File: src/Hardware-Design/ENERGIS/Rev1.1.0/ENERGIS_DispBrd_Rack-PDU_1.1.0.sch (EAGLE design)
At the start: 78 parts, among them CON1 DNI, CON2 AFC11-S20ICC-00, IC1 MCP23017T-E/ML, IC2 MCP23017T-E/ML, T1 DNI

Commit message: general update for the repo
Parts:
- R4: value DNI -> 10K 1%
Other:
- moved on the sheet: DSP
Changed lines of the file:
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@@
 <part name="P+3" library="ds_passive" deviceset="+5V" device=""/>
 <part name="R5" library="ds_resistor" deviceset="33K-1%" device="0402" package3d_urn="urn:adsk.eagle:package:46683744/3" value="33K 1%"/>
-<part name="C7" library="ds_capacitors" deviceset="100NF-25V" device="-0402" package3d_urn="urn:adsk.eagle:package:46766485/3" value="100nF 25V"/>
+<part name="C7" library="ds_capacitors" deviceset="100NF-25V" device="-0402" package3d_urn="urn:adsk.eagle:package:46766485/4" value="100nF 25V"/>
 <part name="GND13" library="ds_passive" deviceset="GND" device=""/>
 <part name="GND17" library="ds_passive" deviceset="GND" device=""/>
 <part name="+3V310" library="ds_passive" deviceset="+3V3" device=""/>
 <part name="R6" library="ds_resistor" deviceset="33K-1%" device="0402" package3d_urn="urn:adsk.eagle:package:46683744/3" value="33K 1%"/>
-<part name="C8" library="ds_capacitors" deviceset="100NF-25V" device="-0402" package3d_urn="urn:adsk.eagle:package:46766485/3" value="100nF 25V"/>
+<part name="C8" library="ds_capacitors" deviceset="100NF-25V" device="-0402" package3d_urn="urn:adsk.eagle:package:46766485/4" value="100nF 25V"/>
 <part name="GND14" library="ds_passive" deviceset="GND" device=""/>
 <part name="GND18" library="ds_passive" deviceset="GND" device=""/>
 <part name="+3V311" library="ds_passive" deviceset="+3V3" device=""/>
 <part name="R12" library="ds_resistor" deviceset="33K-1%" device="0402" package3d_urn="urn:adsk.eagle:package:46683744/3" value="33K 1%"/>
-<part name="C9" library="ds_capacitors" deviceset="100NF-25V" device="-0402" package3d_urn="urn:adsk.eagle:package:46766485/3" value="100nF 25V"/>
+<part name="C9" library="ds_capacitors" deviceset="100NF-25V" device="-0402" package3d_urn="urn:adsk.eagle:package:46766485/4" value="100nF 25V"/>
 <part name="GND19" library="ds_passive" deviceset="GND" device=""/>
 <part name="GND22" library="ds_passive" deviceset="GND" device=""/>
@@
 <part name="+3V38" library="ds_passive" deviceset="+3V3" device=""/>
 <part name="+3V39" library="ds_passive" deviceset="+3V3" device=""/>
-<part name="C5" library="ds_capacitors" deviceset="100NF-25V" device="-0402" package3d_urn="urn:adsk.eagle:package:46766485/3" value="100nF 25V"/>
-<part name="C6" library="ds_capacitors" deviceset="100NF-25V" device="-0402" package3d_urn="urn:adsk.eagle:package:46766485/3" value="100nF 25V"/>
+<part name="C5" library="ds_capacitors" deviceset="100NF-25V" device="-0402" package3d_urn="urn:adsk.eagle:package:46766485/4" value="100nF 25V"/>
+<part name="C6" library="ds_capacitors" deviceset="100NF-25V" device="-0402" package3d_urn="urn:adsk.eagle:package:46766485/4" value="100nF 25V"/>
 <part name="GND12" library="ds_passive" deviceset="GND" device=""/>
 <part name="GND11" library="ds_passive" deviceset="GND" device=""/>
@@
 <part name="NC7" library="ds_passive" library_urn="urn:adsk.eagle:library:46685041" deviceset="NC" device=""/>
 <part name="NC5" library="ds_passive" deviceset="NC" device=""/>
-<part name="R4" library="ds_resistor" deviceset="10K-1%" device="0402" package3d_urn="urn:adsk.eagle:package:46683744/3" value="DNI"/>
+<part name="R4" library="ds_resistor" deviceset="10K-1%" device="0402" package3d_urn="urn:adsk.eagle:package:46683744/3" value="10K 1%"/>
 <part name="GND7" library="ds_passive" deviceset="GND" device=""/>
 <part name="NC8" library="ds_passive" deviceset="NC" device=""/>
-<part name="3V3" library="ds_passive" deviceset="TP" device="-ROUND" value="DNI"/>
-<part name="5V" library="ds_passive" deviceset="TP" device="-ROUND" value="DNI"/>
-<part name="BL" library="ds_passive" deviceset="TP" device="-ROUND" value="DNI"/>
-<part name="GND" library="ds_passive" deviceset="TP" device="-ROUND" value="DNI"/>
+<part name="3V3" library="ds_passive" deviceset="TP" device="-ROUND" package3d_urn="urn:adsk.eagle:package:50081795/1" value="DNI"/>
+<part name="5V" library="ds_passive" deviceset="TP" device="-ROUND" package3d_urn="urn:adsk.eagle:package:50081795/1" value="DNI"/>
+<part name="BL" library="ds_passive" deviceset="TP" device="-ROUND" package3d_urn="urn:adsk.eagle:package:50081795/1" value="DNI"/>
+<part name="GND" library="ds_passive" deviceset="TP" device="-ROUND" package3d_urn="urn:adsk.eagle:package:50081795/1" value="DNI"/>
 <part name="+3V36" library="ds_passive" deviceset="+3V3" device=""/>
 <part name="P+2" library="ds_passive" deviceset="+5V" device=""/>
 <part name="GND10" library="ds_passive" deviceset="GND" device=""/>
 <part name="R13" library="ds_resistor" deviceset="33K-1%" device="0402" package3d_urn="urn:adsk.eagle:package:46683744/3" value="33K 1%"/>
-<part name="C10" library="ds_capacitors" deviceset="100NF-25V" device="-0402" package3d_urn="urn:adsk.eagle:package:46766485/3" value="100nF 25V"/>
+<part name="C10" library="ds_capacitors" deviceset="100NF-25V" device="-0402" package3d_urn="urn:adsk.eagle:package:46766485/4" value="100nF 25V"/>
 <part name="GND24" library="ds_passive" deviceset="GND" device=""/>
 <part name="GND26" library="ds_passive" deviceset="GND" device=""/>
@@
 <part name="+3V2" library="ds_passive" deviceset="+3V3" device=""/>
 <part name="+3V3" library="ds_passive" deviceset="+3V3" device=""/>
-<part name="C11" library="ds_capacitors" deviceset="100NF-25V" device="-0402" package3d_urn="urn:adsk.eagle:package:46766485/3" value="100nF 25V"/>
-<part name="C12" library="ds_capacitors" deviceset="100NF-25V" device="-0402" package3d_urn="urn:adsk.eagle:package:46766485/3" value="100nF 25V"/>
+<part name="C11" library="ds_capacitors" deviceset="100NF-25V" device="-0402" package3d_urn="urn:adsk.eagle:package:46766485/4" value="100nF 25V"/>
+<part name="C12" library="ds_capacitors" deviceset="100NF-25V" device="-0402" package3d_urn="urn:adsk.eagle:package:46766485/4" value="100nF 25V"/>
 <part name="GND27" library="ds_passive" deviceset="GND" device=""/>
 <part name="GND28" library="ds_passive" deviceset="GND" device=""/>
@@
 <part name="O" library="ds_passive" deviceset="SWITCH" device="6X6-SHORT" package3d_urn="urn:adsk.eagle:package:49287357/2" value="TS-1002S-04326C "/>
 <part name="PWR" library="ds_passive" deviceset="SWITCH" device="6X6-SHORT" package3d_urn="urn:adsk.eagle:package:49287357/2" value="TS-1002S-04326C "/>
-<part name="SDA0" library="ds_passive" deviceset="TP" device="-ROUND" value="DNI"/>
-<part name="SCL0" library="ds_passive" deviceset="TP" device="-ROUND" value="DNI"/>
-<part name="MOSI" library="ds_passive" deviceset="TP" device="-ROUND" value="DNI"/>
-<part name="SCK" library="ds_passive" deviceset="TP" device="-ROUND" value="DNI"/>
-<part name="MISO" library="ds_passive" deviceset="TP" device="-ROUND" value="DNI"/>
-<part name="CS" library="ds_passive" deviceset="TP" device="-ROUND" value="DNI"/>
+<part name="SDA0" library="ds_passive" deviceset="TP" device="-ROUND" package3d_urn="urn:adsk.eagle:package:50081795/1" value="DNI"/>
+<part name="SCL0" library="ds_passive" deviceset="TP" device="-ROUND" package3d_urn="urn:adsk.eagle:package:50081795/1" value="DNI"/>
+<part name="MOSI" library="ds_passive" deviceset="TP" device="-ROUND" package3d_urn="urn:adsk.eagle:package:50081795/1" value="DNI"/>
+<part name="SCK" library="ds_passive" deviceset="TP" device="-ROUND" package3d_urn="urn:adsk.eagle:package:50081795/1" value="DNI"/>
+<part name="MISO" library="ds_passive" deviceset="TP" device="-ROUND" package3d_urn="urn:adsk.eagle:package:50081795/1" value="DNI"/>
+<part name="CS" library="ds_passive" deviceset="TP" device="-ROUND" package3d_urn="urn:adsk.eagle:package:50081795/1" value="DNI"/>
 <part name="R16" library="ds_resistor" deviceset="10K-1%" device="0402" package3d_urn="urn:adsk.eagle:package:46683744/3" value="10K 1%"/>
 <part name="R17" library="ds_resistor" deviceset="10K-1%" device="0402" package3d_urn="urn:adsk.eagle:package:46683744/3" value="10K 1%"/>

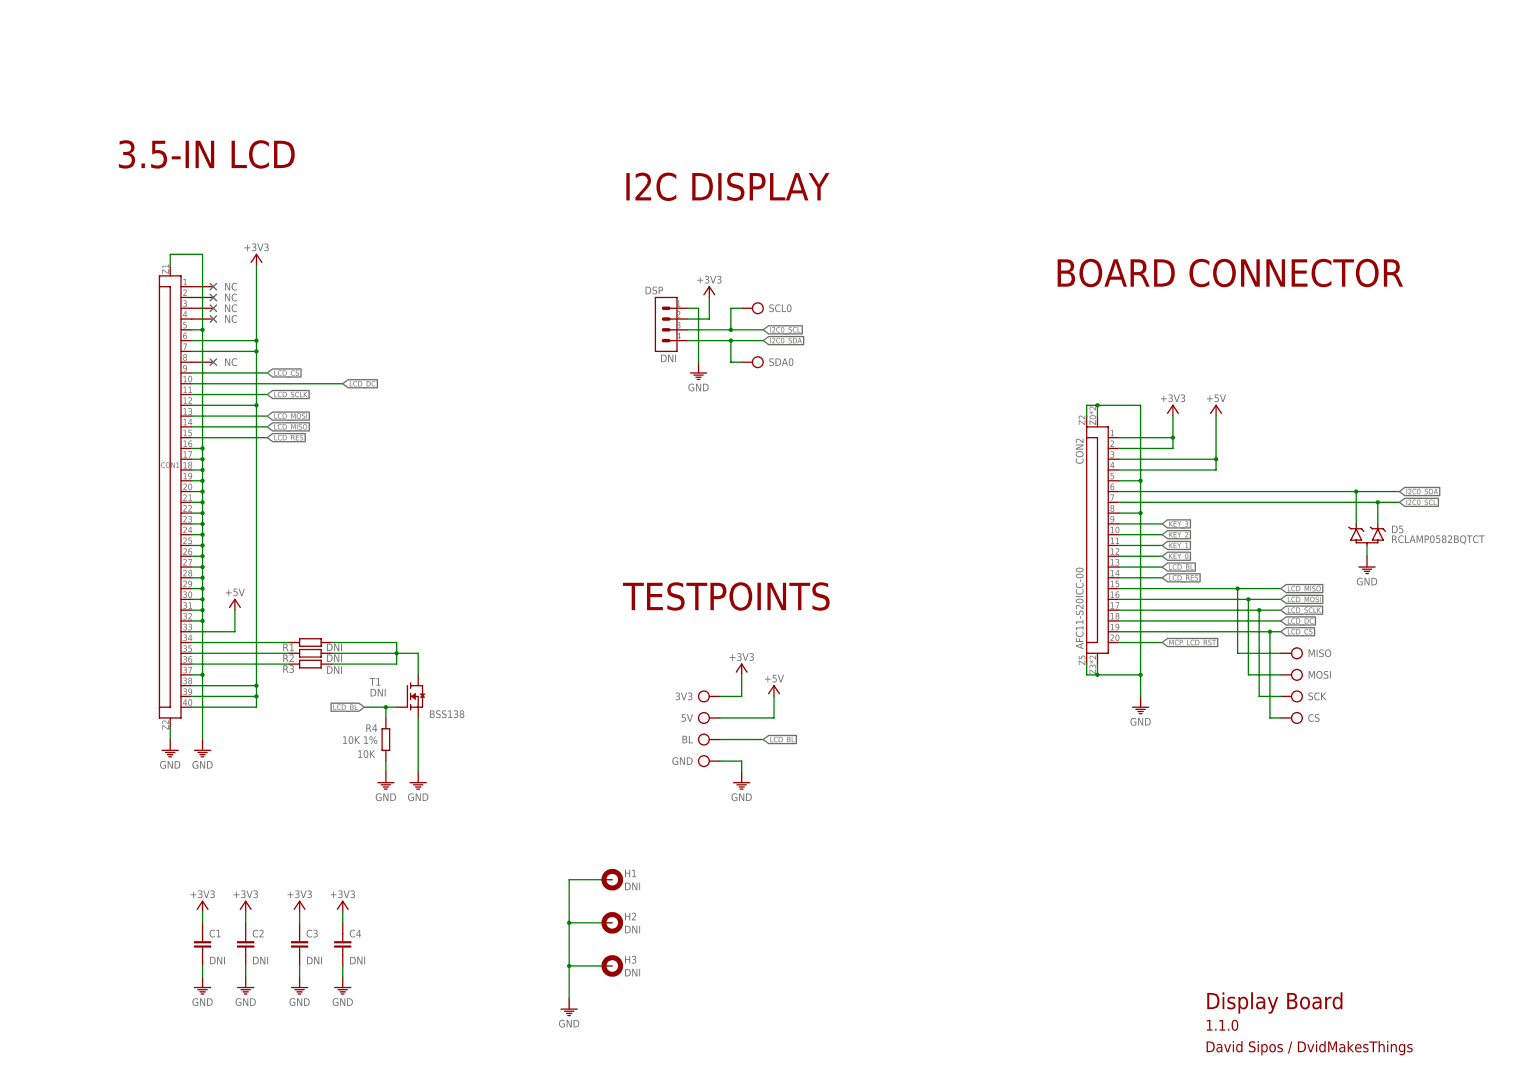
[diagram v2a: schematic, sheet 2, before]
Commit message: add mac calculation
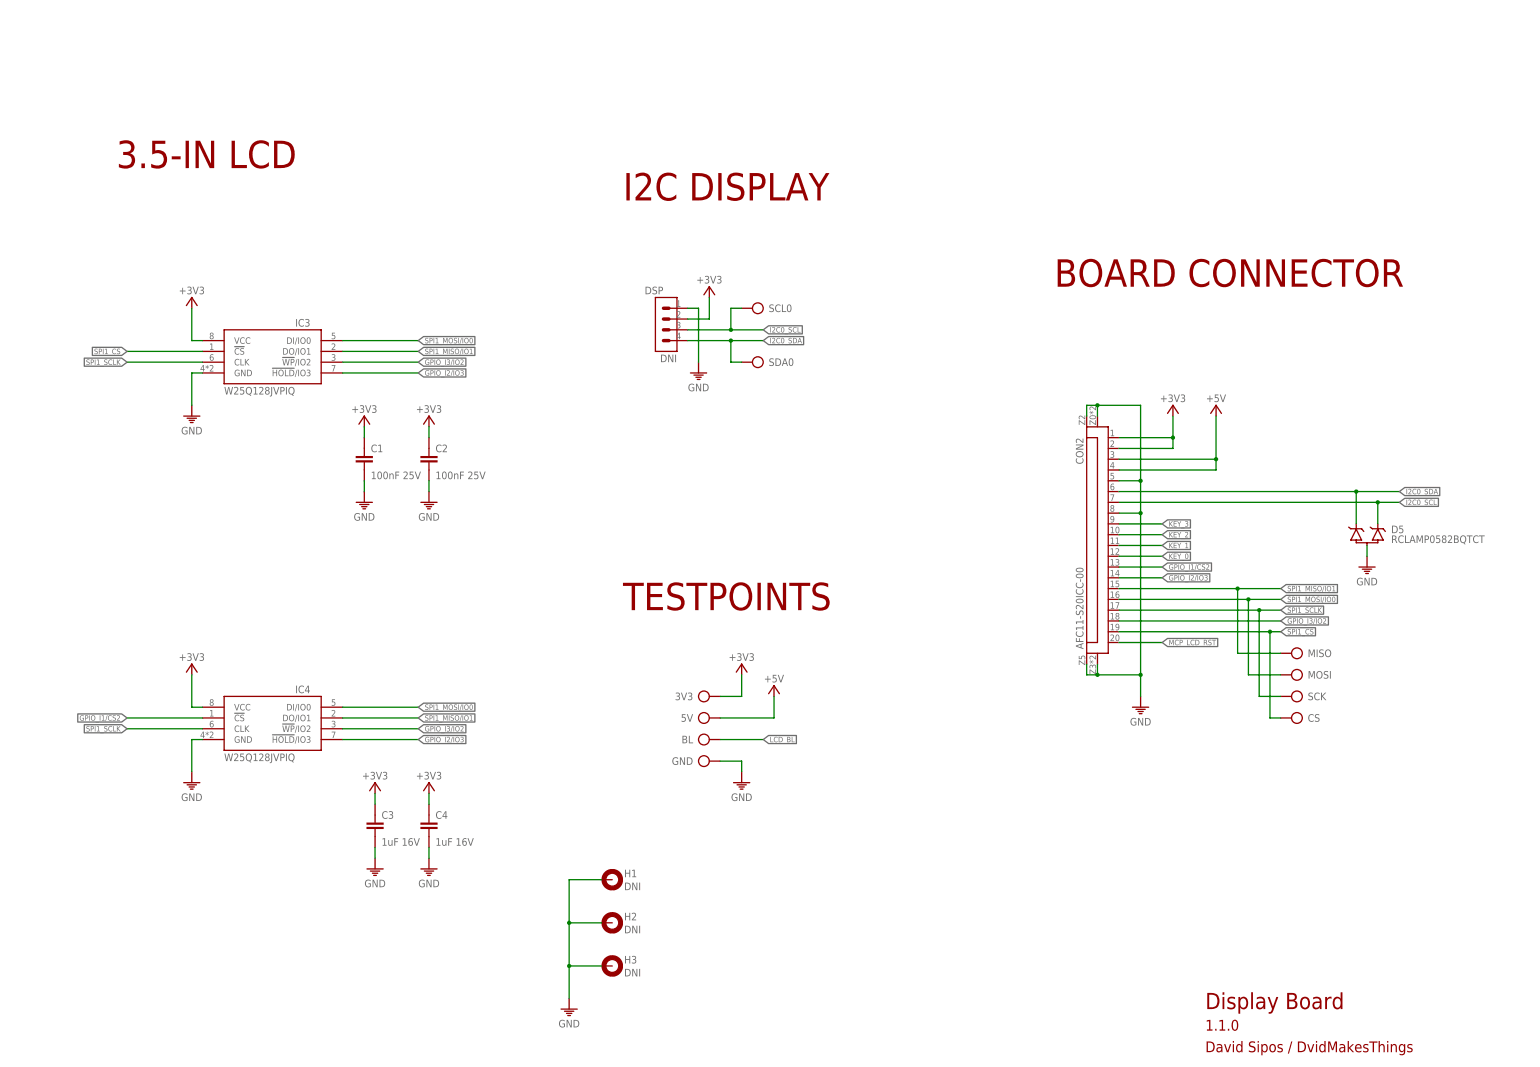
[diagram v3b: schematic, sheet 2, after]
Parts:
- removed CON1: DNI, ds_con:FPC40-HD
- removed R1, R2, R3: DNI, ds_passive:R0402
- removed R4: 10K 1%, ds_resistor:10K-1%0402
- removed T1: DNI, ds_active:BSS138
- added IC3, IC4: W25Q128JVPIQ, ds_ic_memory:W25Q128JVP
- C1, C2: value DNI -> 100nF 25V; device ds_passive:C-0402 -> ds_capacitors:100NF-25V-0402
- C3, C4: value DNI -> 1uF 16V; device ds_passive:C-0402 -> ds_capacitors:1UF-16V0402
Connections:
- removed net LCD_CS: CON1.9, CON2.19, CS.P$1
- removed net LCD_DC: CON1.10, CON2.18
- removed net LCD_MISO: CON1.14, CON2.15, MISO.P$1
- removed net LCD_MOSI: CON1.13, CON2.16, MOSI.P$1
- removed net LCD_RES: CON1.15, CON2.14
- removed net LCD_SCLK: CON1.11, CON2.17, SCK.P$1
- removed net N$2: CON1.35, R2.2
- removed net N$3: CON1.36, R3.2
- removed net N$4: R1.1, R2.1, R3.1, T1.D
- removed net N$5: CON1.34, R1.2
- new net GPIO_I1/CS2: CON2.13, IC4.!CS
- new net GPIO_I2/IO3: CON2.14, IC3.!HOLD!/IO3, IC4.!HOLD!/IO3
- new net GPIO_I3/IO2: CON2.18, IC3.!WP!/IO2, IC4.!WP!/IO2
- new net SPI1_CS: CON2.19, CS.P$1, IC3.!CS
- new net SPI1_MISO/IO1: CON2.15, IC3.DO/IO1, IC4.DO/IO1, MISO.P$1
- new net SPI1_MOSI/IO0: CON2.16, IC3.DI/IO0, IC4.DI/IO0, MOSI.P$1
- new net SPI1_SCLK: CON2.17, IC3.CLK, IC4.CLK, SCK.P$1
- net +3V3: now also IC3.VCC, IC4.VCC; no longer CON1.12, CON1.38, CON1.39, CON1.40, CON1.6, CON1.7
- net +5V: no longer CON1.33
- net GND: now also IC3.GND, IC4.GND; no longer CON1.16, CON1.17, CON1.18, CON1.19, CON1.20, CON1.21, CON1.22, CON1.23, CON1.24, CON1.25, CON1.26, CON1.27, CON1.28, CON1.29, CON1.30, CON1.31, CON1.32, CON1.37, CON1.5, CON1.Z1, CON1.Z2, R4.2, T1.S
- net LCD_BL: no longer CON2.13, R4.1, T1.G
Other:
- note removed: "10K"
- note removed: "BSS138"
- moved on the sheet: C1, C2, C3, C4

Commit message: update documentation
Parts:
- removed IC3, IC4: W25Q128JVPIQ, ds_ic_memory:W25Q128JVP
- added CON1: DNI, ds_con:FPC40-HD
- added R1, R2, R3: DNI, ds_passive:R0402
- added R4: 10K 1%, ds_resistor:10K-1%0402
- added T1: DNI, ds_active:BSS138
- C1, C2: value 100nF 25V -> DNI; device ds_capacitors:100NF-25V-0402 -> ds_passive:C-0402
- C3, C4: value 1uF 16V -> DNI; device ds_capacitors:1UF-16V0402 -> ds_passive:C-0402
- R12, R13, R5, R6: value 33K 1% -> 10K 1%; device ds_resistor:33K-1%0402 -> ds_resistor:10K-1%0402
- R16, R17, R18, R19: value 10K 1% -> 0R 1%; device ds_resistor:10K-1%0402 -> ds_resistor:0R0402
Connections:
- removed net GPIO_I1/CS2: CON2.13, IC4.!CS
- removed net GPIO_I2/IO3: CON2.14, IC3.!HOLD!/IO3, IC4.!HOLD!/IO3
- removed net GPIO_I3/IO2: CON2.18, IC3.!WP!/IO2, IC4.!WP!/IO2
- removed net SPI1_CS: CON2.19, CS.P$1, IC3.!CS
- removed net SPI1_MISO/IO1: CON2.15, IC3.DO/IO1, IC4.DO/IO1, MISO.P$1
- removed net SPI1_MOSI/IO0: CON2.16, IC3.DI/IO0, IC4.DI/IO0, MOSI.P$1
- removed net SPI1_SCLK: CON2.17, IC3.CLK, IC4.CLK, SCK.P$1
- new net LCD_CS: CON1.9, CON2.19, CS.P$1
- new net LCD_DC: CON1.10, CON2.18
- new net LCD_MISO: CON1.14, CON2.15, MISO.P$1
- new net LCD_MOSI: CON1.13, CON2.16, MOSI.P$1
- new net LCD_RES: CON1.15, CON2.14
- new net LCD_SCLK: CON1.11, CON2.17, SCK.P$1
- new net N$2: CON1.35, R2.2
- new net N$3: CON1.36, R3.2
- new net N$4: R1.1, R2.1, R3.1, T1.D
- new net N$5: CON1.34, R1.2
- net +3V3: now also CON1.12, CON1.38, CON1.39, CON1.40, CON1.6, CON1.7; no longer IC3.VCC, IC4.VCC
- net +5V: now also CON1.33
- net GND: now also CON1.16, CON1.17, CON1.18, CON1.19, CON1.20, CON1.21, CON1.22, CON1.23, CON1.24, CON1.25, CON1.26, CON1.27, CON1.28, CON1.29, CON1.30, CON1.31, CON1.32, CON1.37, CON1.5, CON1.Z1, CON1.Z2, R4.2, T1.S; no longer IC3.GND, IC4.GND
- net LCD_BL: now also CON2.13, R4.1, T1.G
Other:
- note added: "10K"
- note added: "BSS138"
- moved on the sheet: C1, C2, C3, C4, DSP
